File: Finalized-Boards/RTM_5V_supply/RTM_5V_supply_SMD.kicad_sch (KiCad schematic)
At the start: 12 parts, among them J1 86093968114755V1LF

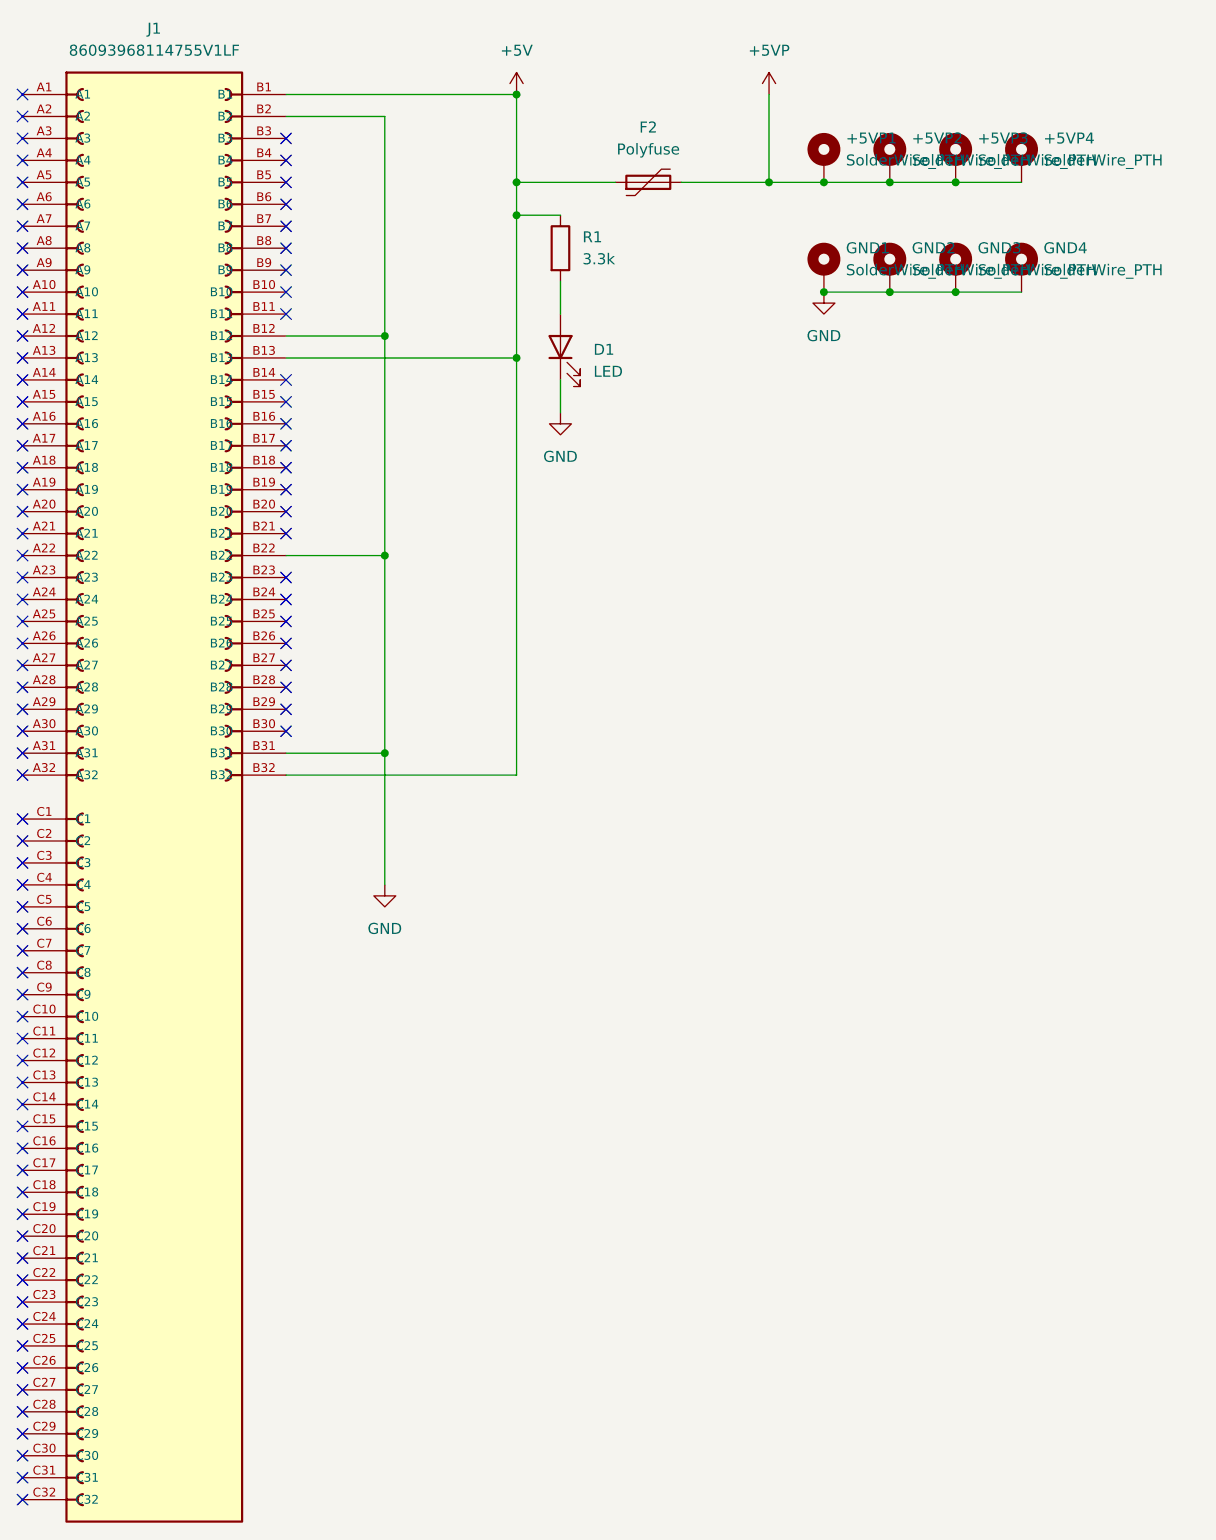
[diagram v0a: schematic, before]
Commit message: Apply Matt's review changes to RTM, fanout and SRAM boards
SRAM: serial -> IDL_26_007 RevC - 09/2026 - CK/RS; vias untented (board-level);
GND zone 0.4 clearance / 0.1524 min width; In2 +3.3V stripe pulled back from
both board edges (tips 103.25 / 126.05) with 45-degree miters; +3.3V via moved
to (165.54, 125.92) and re-routed on F.Cu/B.Cu to clear GND (was 2 DRC errors);
C1/C2 0402 -> 0603 X7R in schematic and PCB; orphan teardrop + 2 zero-length
tracks removed.
Fanout: Matt's reworked layout (12 AWG input centred, both-side labels, 3 mm
shorter test points, D1/R1 as real reference designators, silk moved clear).
RTM: four 1812 1 A PPTCs, one per output; +5V pour full-board on F.Cu/In2,
GND on B.Cu/In1; 3.4 mm fused traces; zones extended past Edge.Cuts.
Removed stale pre-review gerbers/drills/layer PDFs (duplicates of Chris-Originals).
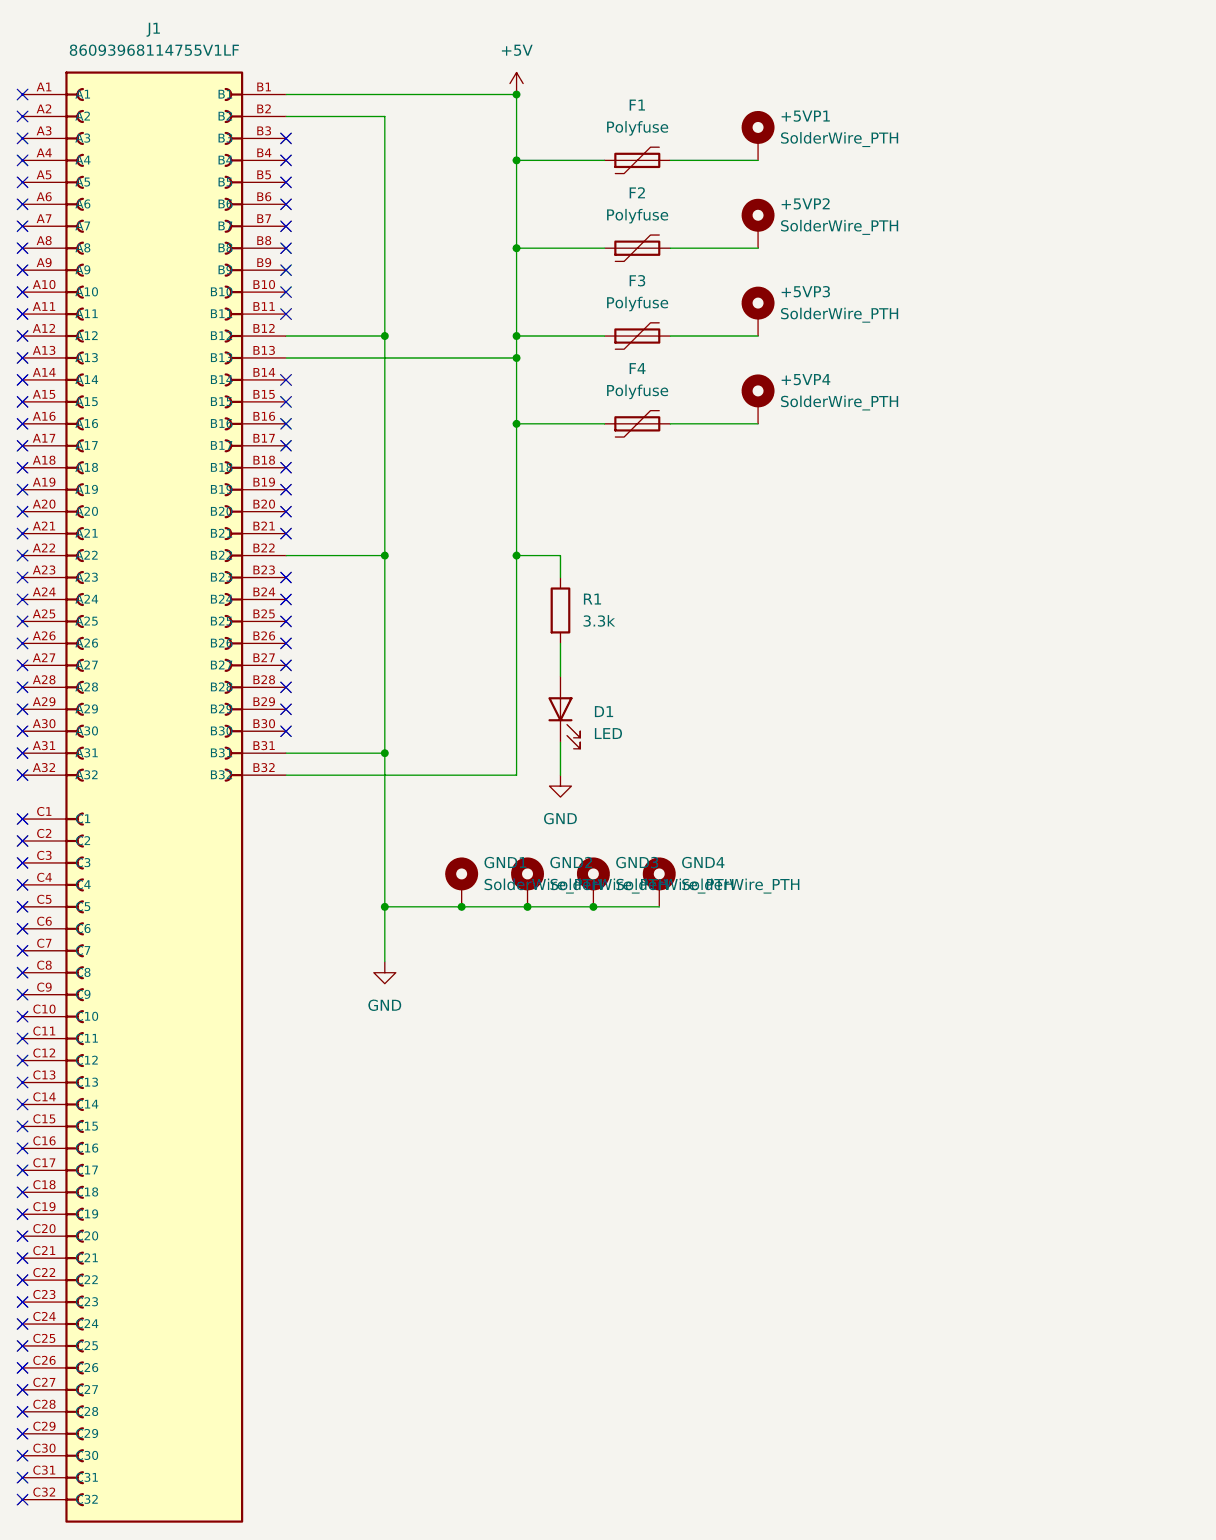
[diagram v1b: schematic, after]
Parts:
- added F1, F3, F4: Polyfuse, Fuse:Fuse_1812_4532Metric, symbol Device:Polyfuse
- F2: footprint Fuse:Fuse_Bourns_MF-RHT100 -> Fuse:Fuse_1812_4532Metric
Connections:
- net +5V: now also F1.1, F3.1, F4.1
- removed net +5VP: +5VP1.1, +5VP2.1, +5VP3.1, +5VP4.1, F2.2
- new net: +5VP2.1, F2.2
- new net: +5VP3.1, F3.2
- new net: +5VP1.1, F1.2
- new net: +5VP4.1, F4.2
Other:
- moved on the sheet: +5VP1, +5VP2, +5VP3, +5VP4, D1, F2, GND1, GND2, GND3, GND4, R1

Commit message: Matt follow-up: 3.3V zone 0.4 clearance, silk-over-copper ignored, RTM IDL_26_026 silkscreen, fuse part MF-MSMF110/16-2
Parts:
- F1, F2, F3, F4: value Polyfuse -> MF-MSMF110/16-2
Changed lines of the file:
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@@
 			)
 		)
-		(property "Value" "Polyfuse"
+		(property "Value" "MF-MSMF110/16-2"
 			(at 199.39 36.83 90)
 			(show_name no)
@@
 			)
 		)
-		(property "Value" "Polyfuse"
+		(property "Value" "MF-MSMF110/16-2"
 			(at 199.39 46.99 90)
 			(show_name no)
@@
 			)
 		)
-		(property "Value" "Polyfuse"
+		(property "Value" "MF-MSMF110/16-2"
 			(at 199.39 26.67 90)
 			(show_name no)
@@
 			)
 		)
-		(property "Value" "Polyfuse"
+		(property "Value" "MF-MSMF110/16-2"
 			(at 199.39 57.15 90)
 			(show_name no)

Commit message: Polyswitches sized to load: RTM F1-F4 MF-MSMF110/16-2 -> MF-MSMF030-2 (0.3 A), fanout F1-F4 -> MF-MSMF010-2 (0.1 A); refresh renders and DRC
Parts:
- F1, F2, F3, F4: value MF-MSMF110/16-2 -> MF-MSMF030-2
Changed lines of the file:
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@@
 			)
 		)
-		(property "Value" "MF-MSMF110/16-2"
+		(property "Value" "MF-MSMF030-2"
 			(at 199.39 36.83 90)
 			(show_name no)
@@
 			)
 		)
-		(property "Value" "MF-MSMF110/16-2"
+		(property "Value" "MF-MSMF030-2"
 			(at 199.39 46.99 90)
 			(show_name no)
@@
 			)
 		)
-		(property "Value" "MF-MSMF110/16-2"
+		(property "Value" "MF-MSMF030-2"
 			(at 199.39 26.67 90)
 			(show_name no)
@@
 			)
 		)
-		(property "Value" "MF-MSMF110/16-2"
+		(property "Value" "MF-MSMF030-2"
 			(at 199.39 57.15 90)
 			(show_name no)
